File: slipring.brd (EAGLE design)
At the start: 65 x 65 mm, 4 parts

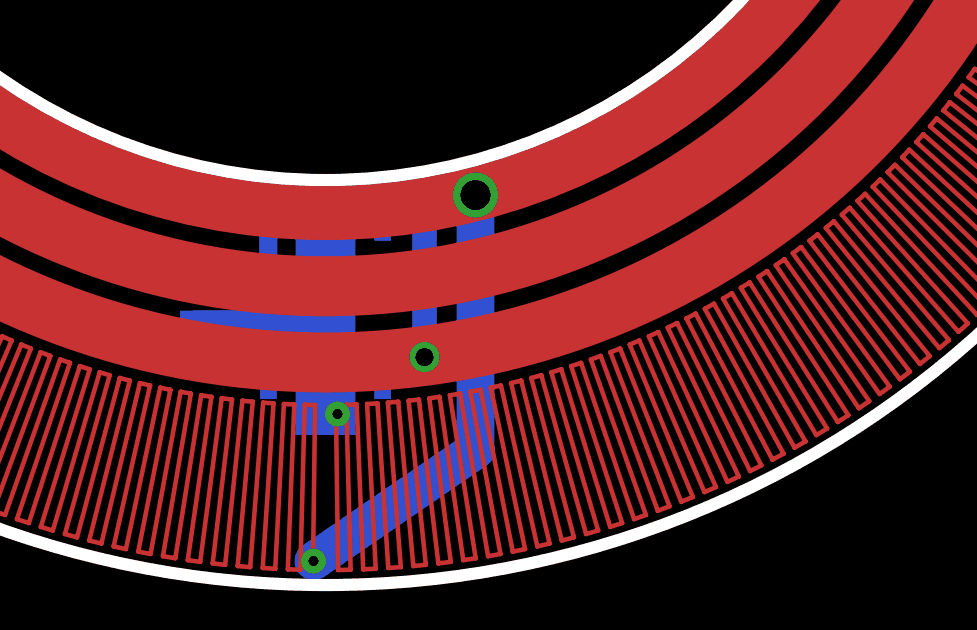
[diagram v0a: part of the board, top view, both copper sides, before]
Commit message: switched to 20mA reg
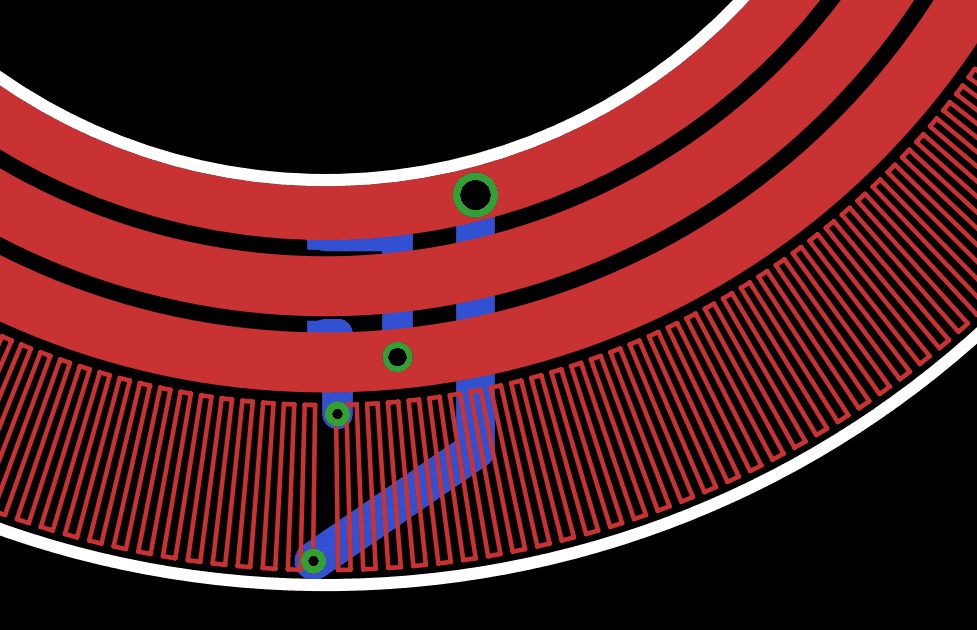
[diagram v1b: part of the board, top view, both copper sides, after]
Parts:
- removed R1: 67, resistor:R0603
- removed REG: LM334MX, CUSTOM:8-SOIC
- added CCR: CCR, CUSTOM:CCR
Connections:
- removed net N$8: R1.2, REG.1
- removed net N$9: R1.1, REG.2, U$2.D
- new net N$3: CCR.OUT, U$2.D
- net VCC: now also CCR.IN; no longer REG.4
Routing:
- net N$9: track 15.5 -> 0.00 mm
- net N$8: track 4.29 -> 0.00 mm
- net N$3: track 0.00 -> 3.06 mm
- net VCC: track 82.7 -> 84.0 mm
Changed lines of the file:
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@@
 <circle x="32.5" y="32.5" radius="19" width="0.4064" layer="20"/>
 <circle x="32.5" y="32.5" radius="32.5" width="0.4064" layer="20"/>
-<rectangle x1="31.5" y1="5" x2="33.5" y2="13" layer="16"/>
 </plain>
 <attributes>
@@
 </autorouter>
 <elements>
-<element name="R1" library="resistor" package="R0603" value="67" x="28.2" y="9.5" smashed="yes" rot="MR90">
-<attribute name="NAME" x="25.835" y="8.865" size="1.27" layer="26" rot="MR90"/>
-<attribute name="VALUE" x="26.295" y="8.865" size="1.27" layer="28" rot="MR90"/>
-</element>
-<element name="REG" library="CUSTOM" package="8-SOIC" value="LM334MX" x="32.5" y="9.6" smashed="yes" rot="MR270">
-<attribute name="NAME" x="35.945" y="7.1456" size="2.0828" layer="26" ratio="10" rot="SMR90"/>
-<attribute name="VALUE" x="38.215" y="13.0544" size="2.0828" layer="28" ratio="10" rot="SMR270"/>
-</element>
 <element name="CONN" library="CUSTOM" package="BOURNS_2PIN" value="BOURNS_2PIN" x="32.5" y="56" rot="MR270"/>
 <element name="U$2" library="CUSTOM" package="RING3" value="RING3" x="32.5" y="32.5"/>
+<element name="CCR" library="CUSTOM" package="CCR" value="CCR" x="32.5" y="10" smashed="yes" rot="MR90">
+<attribute name="NAME" x="30.2" y="8.6" size="1.016" layer="26" rot="MR90"/>
+</element>
 </elements>
 <signals>
@@
 </signal>
 <signal name="VCC">
-<contactref element="REG" pad="4"/>
 <contactref element="CONN" pad="P$1"/>
 <contactref element="U$2" pad="V+"/>
-<wire x1="34.405" y1="12.2416" x2="35.8" y2="12.2416" width="0.8128" layer="16"/>
-<wire x1="35.8" y1="12.2416" x2="35.8" y2="7.6" width="0.8128" layer="16"/>
-<via x="35.8" y="7.6" extent="1-16" drill="0.6"/>
-<wire x1="35.8" y1="7.6" x2="48" y2="12" width="0.4064" layer="1"/>
+<via x="34.9" y="7.6" extent="1-16" drill="0.6"/>
+<wire x1="34.9" y1="7.6" x2="48" y2="12" width="0.4064" layer="1"/>
 <wire x1="48" y1="12" x2="55" y2="22" width="0.4064" layer="1"/>
 <wire x1="55" y1="22" x2="58" y2="31" width="0.4064" layer="1"/>
@@
 <wire x1="38" y1="57" x2="32.5" y2="57.58" width="0.4064" layer="1"/>
 <wire x1="31.53" y1="57.27" x2="32.5" y2="57.58" width="1.016" layer="16"/>
-</signal>
-<signal name="N$8">
-<contactref element="REG" pad="1"/>
-<contactref element="R1" pad="2"/>
-<wire x1="28.2" y1="10.35" x2="30.595" y2="10.35" width="0.6096" layer="16"/>
-<wire x1="30.595" y1="10.35" x2="30.595" y2="12.2416" width="0.6096" layer="16"/>
-</signal>
-<signal name="N$9">
-<contactref element="R1" pad="1"/>
-<contactref element="REG" pad="2"/>
-<wire x1="28.2" y1="8.65" x2="32" y2="8.65" width="1.016" layer="16"/>
-<wire x1="32" y1="8.65" x2="32.7" y2="8.65" width="1.016" layer="16"/>
-<wire x1="31.865" y1="12.2416" x2="32" y2="12.2416" width="0.254" layer="16"/>
-<wire x1="32" y1="12.2416" x2="32" y2="8.65" width="0.254" layer="16"/>
-<contactref element="U$2" pad="D"/>
-<wire x1="28.2" y1="8.65" x2="32.7" y2="8.5" width="0.4064" layer="16"/>
-<wire x1="32.7" y1="8.5" x2="32.9" y2="5.7" width="0.4064" layer="16"/>
+<contactref element="CCR" pad="IN"/>
+<wire x1="34.9" y1="7.6" x2="34.9" y2="11.6375" width="1.016" layer="16"/>
+<wire x1="34.9" y1="11.6375" x2="32.5" y2="11.6375" width="1.016" layer="16"/>
 </signal>
 <signal name="AGND">
@@
 <wire x1="32" y1="54.73" x2="39" y2="54.73" width="1.27" layer="16"/>
 </signal>
+<signal name="N$3">
+<contactref element="U$2" pad="D"/>
+<contactref element="CCR" pad="OUT"/>
+<wire x1="32.5" y1="8.3625" x2="32.9" y2="8.3625" width="1.016" layer="16"/>
+<wire x1="32.9" y1="8.3625" x2="32.9" y2="5.7" width="1.016" layer="16"/>
+</signal>
 </signals>

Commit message: final cad for purchase
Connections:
- net GND: now also CONN.P2; no longer CONN.P$2
- net VCC: now also CONN.P1; no longer CONN.P$1
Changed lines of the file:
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@@
 </class>
 </classes>
-<designrules name="default">
+<designrules name="default *">
 <description language="de">&lt;b&gt;EAGLE Design Rules&lt;/b&gt;
 &lt;p&gt;
@@
 <param name="msMicroVia" value="9.99mm"/>
 <param name="msBlindViaRatio" value="0.5"/>
-<param name="rvPadTop" value="0.25"/>
-<param name="rvPadInner" value="0.25"/>
-<param name="rvPadBottom" value="0.25"/>
-<param name="rvViaOuter" value="0.25"/>
-<param name="rvViaInner" value="0.25"/>
-<param name="rvMicroViaOuter" value="0.25"/>
-<param name="rvMicroViaInner" value="0.25"/>
-<param name="rlMinPadTop" value="10mil"/>
+<param name="rvPadTop" value="0"/>
+<param name="rvPadInner" value="0"/>
+<param name="rvPadBottom" value="0"/>
+<param name="rvViaOuter" value="0"/>
+<param name="rvViaInner" value="0"/>
+<param name="rvMicroViaOuter" value="0"/>
+<param name="rvMicroViaInner" value="0"/>
+<param name="rlMinPadTop" value="0mil"/>
 <param name="rlMaxPadTop" value="20mil"/>
-<param name="rlMinPadInner" value="10mil"/>
+<param name="rlMinPadInner" value="0mil"/>
 <param name="rlMaxPadInner" value="20mil"/>
-<param name="rlMinPadBottom" value="10mil"/>
+<param name="rlMinPadBottom" value="0mil"/>
 <param name="rlMaxPadBottom" value="20mil"/>
-<param name="rlMinViaOuter" value="8mil"/>
+<param name="rlMinViaOuter" value="0mil"/>
 <param name="rlMaxViaOuter" value="20mil"/>
-<param name="rlMinViaInner" value="8mil"/>
+<param name="rlMinViaInner" value="0mil"/>
 <param name="rlMaxViaInner" value="20mil"/>
-<param name="rlMinMicroViaOuter" value="4mil"/>
+<param name="rlMinMicroViaOuter" value="0mil"/>
 <param name="rlMaxMicroViaOuter" value="20mil"/>
-<param name="rlMinMicroViaInner" value="4mil"/>
+<param name="rlMinMicroViaInner" value="0mil"/>
 <param name="rlMaxMicroViaInner" value="20mil"/>
 <param name="psTop" value="-1"/>
@@
 <signals>
 <signal name="GND">
-<contactref element="CONN" pad="P$2"/>
+<contactref element="CONN" pad="P2"/>
 <contactref element="U$2" pad="GND"/>
 <wire x1="31.53" y1="54.73" x2="32.5" y2="55.04" width="1.016" layer="16"/>
 </signal>
 <signal name="VCC">
-<contactref element="CONN" pad="P$1"/>
+<contactref element="CONN" pad="P1"/>
 <contactref element="U$2" pad="V+"/>
 <via x="34.9" y="7.6" extent="1-16" drill="0.6"/>
@@
 <contactref element="CCR" pad="OUT"/>
 <wire x1="32.5" y1="8.3625" x2="32.9" y2="8.3625" width="1.016" layer="16"/>
-<wire x1="32.9" y1="8.3625" x2="32.9" y2="5.7" width="1.016" layer="16"/>
+<wire x1="32.9" y1="8.3625" x2="32.8" y2="5.7" width="1.016" layer="16"/>
 </signal>
 </signals>

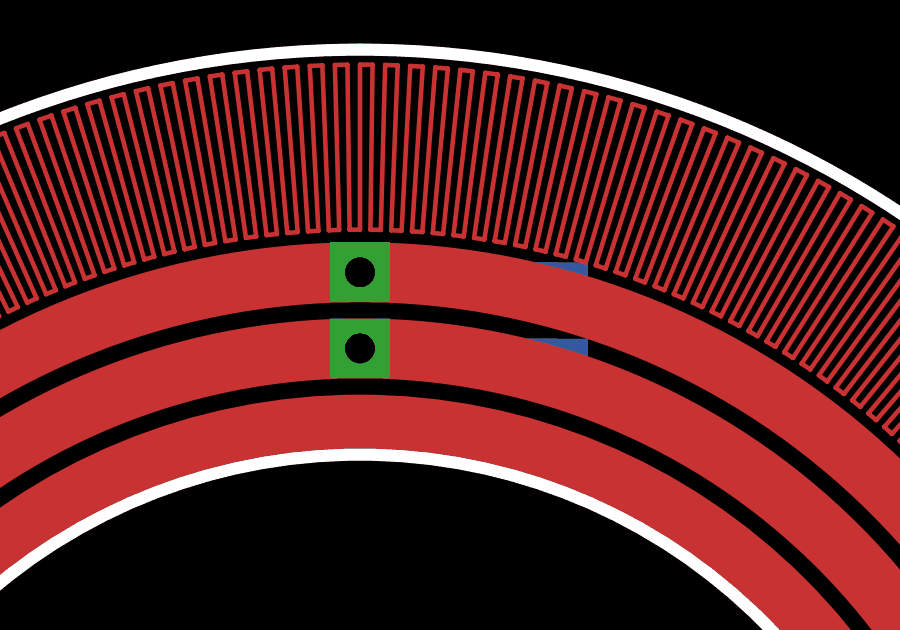
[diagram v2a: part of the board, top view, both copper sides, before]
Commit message: fixed intial board errors, including short, flipped usb, and missing trace
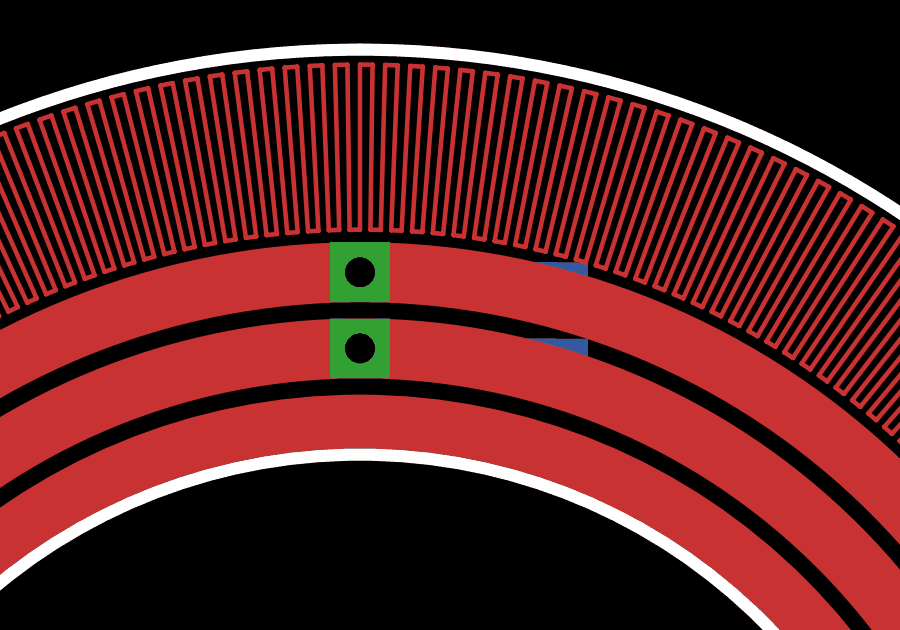
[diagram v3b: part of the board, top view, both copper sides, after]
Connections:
- net GND: now also CONN.P3
- net VCC: now also CONN.P4
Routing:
- net N$2: track 7.00 -> 0.00 mm
- net N$1: track 7.00 -> 0.00 mm
- net VCC: track 84.0 -> 90.7 mm
- net GND: track 1.02 -> 7.80 mm
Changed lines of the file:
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@@
 <contactref element="U$2" pad="GND"/>
 <wire x1="31.53" y1="54.73" x2="32.5" y2="55.04" width="1.016" layer="16"/>
+<contactref element="CONN" pad="P3"/>
+<wire x1="38.97" y1="54.73" x2="32.5" y2="54.73" width="1.27" layer="16"/>
+<wire x1="32.5" y1="54.73" x2="32.5" y2="55.04" width="1.27" layer="16"/>
 </signal>
 <signal name="VCC">
@@
 <wire x1="34.9" y1="7.6" x2="34.9" y2="11.6375" width="1.016" layer="16"/>
 <wire x1="34.9" y1="11.6375" x2="32.5" y2="11.6375" width="1.016" layer="16"/>
+<contactref element="CONN" pad="P4"/>
+<wire x1="38.97" y1="57.27" x2="32.5" y2="57.27" width="1.27" layer="16"/>
+<wire x1="32.5" y1="57.27" x2="32.5" y2="57.58" width="1.27" layer="16"/>
 </signal>
 <signal name="AGND">
 <contactref element="U$2" pad="AGND"/>
 </signal>
-<signal name="N$1">
-<wire x1="39" y1="57.27" x2="32" y2="57.27" width="1.27" layer="16"/>
-</signal>
-<signal name="N$2">
-<wire x1="32" y1="54.73" x2="39" y2="54.73" width="1.27" layer="16"/>
-</signal>
 <signal name="N$3">
